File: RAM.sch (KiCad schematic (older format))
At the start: 9 parts

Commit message: Minor fixes and the gitignore was removed
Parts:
- added C?: 100n, symbol C
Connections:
- net +3V3: no longer C?.1, C?.1, U?.1 (VDD), U?.25 (VDD)
- net GNDD: now also C?.2
- net at C?.1, C?.1, C?.1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: now also C?.1, C?.1, U?.1 (VDD), U?.25 (VDD), C?.1
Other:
- moved on the sheet: C?
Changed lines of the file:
@@
 L C C?
 U 1 1 58E1D705
-P 4600 1350
-F 0 "C?" H 4625 1450 50  0000 L CNN
-F 1 "2.7u" H 4625 1250 50  0000 L CNN
-F 2 "" H 4638 1200 50  0001 C CNN
-F 3 "" H 4600 1350 50  0001 C CNN
-	1    4600 1350
+P 4600 1400
+F 0 "C?" H 4625 1500 50  0000 L CNN
+F 1 "2.7u" H 4625 1300 50  0000 L CNN
+F 2 "" H 4638 1250 50  0001 C CNN
+F 3 "" H 4600 1400 50  0001 C CNN
+	1    4600 1400
 	1    0    0    -1
 $EndComp
@@
 L C C?
 U 1 1 58E1D776
-P 4400 1350
-F 0 "C?" H 4425 1450 50  0000 L CNN
-F 1 "100n" H 4425 1250 50  0000 L CNN
-F 2 "" H 4438 1200 50  0001 C CNN
-F 3 "" H 4400 1350 50  0001 C CNN
-	1    4400 1350
+P 4400 1400
+F 0 "C?" H 4425 1500 50  0000 L CNN
+F 1 "100n" H 4425 1300 50  0000 L CNN
+F 2 "" H 4438 1250 50  0001 C CNN
+F 3 "" H 4400 1400 50  0001 C CNN
+	1    4400 1400
 	1    0    0    -1
 $EndComp
@@
 L GNDD #PWR?
 U 1 1 58E1D898
-P 4500 1500
-F 0 "#PWR?" H 4500 1250 50  0001 C CNN
-F 1 "GNDD" H 4500 1350 50  0000 C CNN
-F 2 "" H 4500 1500 50  0001 C CNN
-F 3 "" H 4500 1500 50  0001 C CNN
-	1    4500 1500
+P 4500 1600
+F 0 "#PWR?" H 4500 1350 50  0001 C CNN
+F 1 "GNDD" H 4500 1450 50  0000 C CNN
+F 2 "" H 4500 1600 50  0001 C CNN
+F 3 "" H 4500 1600 50  0001 C CNN
+	1    4500 1600
 	1    0    0    -1
 $EndComp
@@
 	4750 4900 4750 4750
 Wire Wire Line
-	4750 4750 5250 4750
-Connection ~ 4850 4750
-Connection ~ 4950 4750
-Connection ~ 5050 4750
-Connection ~ 5150 4750
-Wire Wire Line
 	5350 1200 5500 1200
 Wire Wire Line
-	3750 1200 5050 1200
+	3500 1200 5050 1200
 Connection ~ 4600 1200
-Wire Wire Line
-	4750 1650 5050 1650
 Wire Wire Line
 	4950 1650 4950 1200
 Connection ~ 4950 1200
-Wire Wire Line
-	5450 1650 5450 1200
 Connection ~ 5450 1200
-Wire Wire Line
-	3750 1500 4600 1500
-Connection ~ 4500 1500
-Connection ~ 4850 1650
+$Comp
+L C C?
+U 1 1 58E1DAA0
+P 3750 1400
+F 0 "C?" H 3775 1500 50  0000 L CNN
+F 1 "100n" H 3775 1300 50  0000 L CNN
+F 2 "" H 3788 1250 50  0001 C CNN
+F 3 "" H 3750 1400 50  0001 C CNN
+	1    3750 1400
+	1    0    0    -1
+$EndComp
+$Comp
+L C C?
+U 1 1 58E1DADF
+P 3950 1400
+F 0 "C?" H 3975 1500 50  0000 L CNN
+F 1 "100n" H 3975 1300 50  0000 L CNN
+F 2 "" H 3988 1250 50  0001 C CNN
+F 3 "" H 3950 1400 50  0001 C CNN
+	1    3950 1400
+	1    0    0    -1
+$EndComp
+$Comp
+L C C?
+U 1 1 58E1DB0D
+P 4200 1400
+F 0 "C?" H 4225 1500 50  0000 L CNN
+F 1 "100n" H 4225 1300 50  0000 L CNN
+F 2 "" H 4238 1250 50  0001 C CNN
+F 3 "" H 4200 1400 50  0001 C CNN
+	1    4200 1400
+	1    0    0    -1
+$EndComp
+Connection ~ 3950 1200
+Connection ~ 4400 1200
+$Comp
+L C C?
+U 1 1 58E1DD36
+P 5600 1600
+F 0 "C?" H 5625 1700 50  0000 L CNN
+F 1 "100n" H 5625 1500 50  0000 L CNN
+F 2 "" H 5638 1450 50  0001 C CNN
+F 3 "" H 5600 1600 50  0001 C CNN
+	1    5600 1600
+	1    0    0    -1
+$EndComp
+$Comp
+L GNDD #PWR?
+U 1 1 58E1DD7E
+P 5950 1850
+F 0 "#PWR?" H 5950 1600 50  0001 C CNN
+F 1 "GNDD" H 5950 1700 50  0000 C CNN
+F 2 "" H 5950 1850 50  0001 C CNN
+F 3 "" H 5950 1850 50  0001 C CNN
+	1    5950 1850
+	1    0    0    -1
+$EndComp
+$Comp
+L C C?
+U 1 1 58E1DDA1
+P 5950 1600
+F 0 "C?" H 5975 1700 50  0000 L CNN
+F 1 "100n" H 5975 1500 50  0000 L CNN
+F 2 "" H 5988 1450 50  0001 C CNN
+F 3 "" H 5950 1600 50  0001 C CNN
+	1    5950 1600
+	1    0    0    -1
+$EndComp
+Wire Wire Line
+	4950 1400 5950 1400
+Connection ~ 5600 1400
+Wire Wire Line
+	3750 1250 3750 1200
+Wire Wire Line
+	3950 1250 3950 1200
+Wire Wire Line
+	4400 1250 4400 1200
+Wire Wire Line
+	4600 1250 4600 1200
+Wire Wire Line
+	4600 1600 4600 1550
+Wire Wire Line
+	3500 1600 4600 1600
+Wire Wire Line
+	3750 1600 3750 1550
+Connection ~ 4500 1600
+Wire Wire Line
+	3950 1550 3950 1600
+Connection ~ 3950 1600
+Wire Wire Line
+	4400 1550 4400 1600
+Connection ~ 4400 1600
+Wire Wire Line
+	4200 1250 4200 1200
+Connection ~ 4200 1200
+Wire Wire Line
+	4200 1550 4200 1600
+Connection ~ 4200 1600
+$Comp
+L C C?
+U 1 1 58DF4B0B
+P 3500 1400
+F 0 "C?" H 3525 1500 50  0000 L CNN
+F 1 "100n" H 3525 1300 50  0000 L CNN
+F 2 "" H 3538 1250 50  0001 C CNN
+F 3 "" H 3500 1400 50  0001 C CNN
+	1    3500 1400
+	1    0    0    -1
+$EndComp
+Wire Wire Line
+	3500 1200 3500 1250
+Connection ~ 3750 1200
+Wire Wire Line
+	3500 1600 3500 1550
+Connection ~ 3750 1600
+Wire Wire Line
+	5600 1450 5600 1400
+Wire Wire Line
+	5950 1400 5950 1450
+Wire Wire Line
+	5950 1750 5950 1850
+Wire Wire Line
+	5950 1800 5600 1800
+Wire Wire Line
+	5600 1800 5600 1750
+Connection ~ 5950 1800
+Wire Wire Line
+	4750 1650 4750 1550
+Wire Wire Line
+	4750 1550 5250 1550
+Connection ~ 4950 1550
+Wire Wire Line
+	5250 1550 5250 1650
+Connection ~ 4950 1400
+Wire Wire Line
+	4850 1650 4850 1550
+Connection ~ 4850 1550
+Wire Wire Line
+	5050 1650 5050 1550
+Connection ~ 5050 1550
+Wire Wire Line
+	5150 1650 5150 1550
+Connection ~ 5150 1550
+Wire Wire Line
+	5250 4750 5250 4850
+Wire Wire Line
+	5250 4850 4750 4850
+Connection ~ 4750 4850
 $Comp
 L AS4C1M16S U?
@@
 	1    0    0    -1
 $EndComp
-Connection ~ 4950 1650
-Wire Wire Line
-	5150 1650 5450 1650
-Connection ~ 5250 1650
-Connection ~ 4750 1650
-$Comp
-L C C?
-U 1 1 58E1DAA0
-P 3750 1350
-F 0 "C?" H 3775 1450 50  0000 L CNN
-F 1 "100n" H 3775 1250 50  0000 L CNN
-F 2 "" H 3788 1200 50  0001 C CNN
-F 3 "" H 3750 1350 50  0001 C CNN
-	1    3750 1350
-	1    0    0    -1
-$EndComp
-$Comp
-L C C?
-U 1 1 58E1DADF
-P 3950 1350
-F 0 "C?" H 3975 1450 50  0000 L CNN
-F 1 "100n" H 3975 1250 50  0000 L CNN
-F 2 "" H 3988 1200 50  0001 C CNN
-F 3 "" H 3950 1350 50  0001 C CNN
-	1    3950 1350
-	1    0    0    -1
-$EndComp
-$Comp
-L C C?
-U 1 1 58E1DB0D
-P 4150 1350
-F 0 "C?" H 4175 1450 50  0000 L CNN
-F 1 "100n" H 4175 1250 50  0000 L CNN
-F 2 "" H 4188 1200 50  0001 C CNN
-F 3 "" H 4150 1350 50  0001 C CNN
-	1    4150 1350
-	1    0    0    -1
-$EndComp
-Connection ~ 3950 1200
-Connection ~ 4150 1200
-Connection ~ 4400 1200
-Connection ~ 3950 1500
-Connection ~ 4400 1500
-Connection ~ 4150 1500
-$Comp
-L C C?
-U 1 1 58E1DD36
-P 5600 1550
-F 0 "C?" H 5625 1650 50  0000 L CNN
-F 1 "100n" H 5625 1450 50  0000 L CNN
-F 2 "" H 5638 1400 50  0001 C CNN
-F 3 "" H 5600 1550 50  0001 C CNN
-	1    5600 1550
-	1    0    0    -1
-$EndComp
-$Comp
-L GNDD #PWR?
-U 1 1 58E1DD7E
-P 5600 1700
-F 0 "#PWR?" H 5600 1450 50  0001 C CNN
-F 1 "GNDD" H 5600 1550 50  0000 C CNN
-F 2 "" H 5600 1700 50  0001 C CNN
-F 3 "" H 5600 1700 50  0001 C CNN
-	1    5600 1700
-	1    0    0    -1
-$EndComp
-$Comp
-L C C?
-U 1 1 58E1DDA1
-P 5950 1550
-F 0 "C?" H 5975 1650 50  0000 L CNN
-F 1 "100n" H 5975 1450 50  0000 L CNN
-F 2 "" H 5988 1400 50  0001 C CNN
-F 3 "" H 5950 1550 50  0001 C CNN
-	1    5950 1550
-	1    0    0    -1
-$EndComp
-Wire Wire Line
-	5600 1700 5950 1700
-Wire Wire Line
-	5450 1400 5950 1400
-Connection ~ 5450 1400
-Connection ~ 5600 1400
+Wire Wire Line
+	4850 4750 4850 4850
+Connection ~ 4850 4850
+Wire Wire Line
+	4950 4750 4950 4850
+Connection ~ 4950 4850
+Wire Wire Line
+	5050 4750 5050 4850
+Connection ~ 5050 4850
+Wire Wire Line
+	5150 4750 5150 4850
+Connection ~ 5150 4850
 $EndSCHEMATC

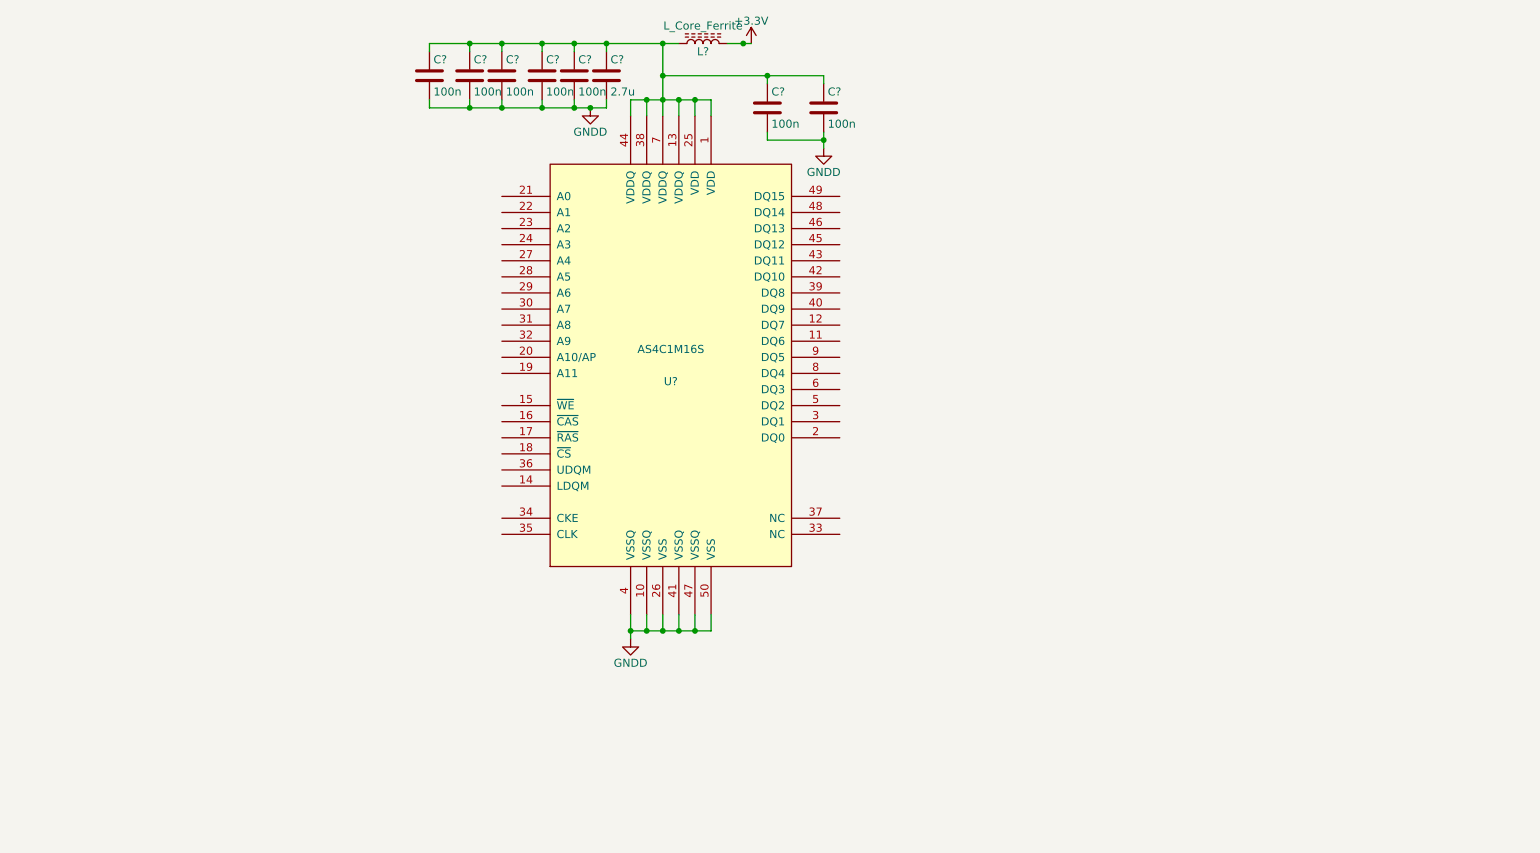
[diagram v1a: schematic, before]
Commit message: Reordered IO connections to FPGA
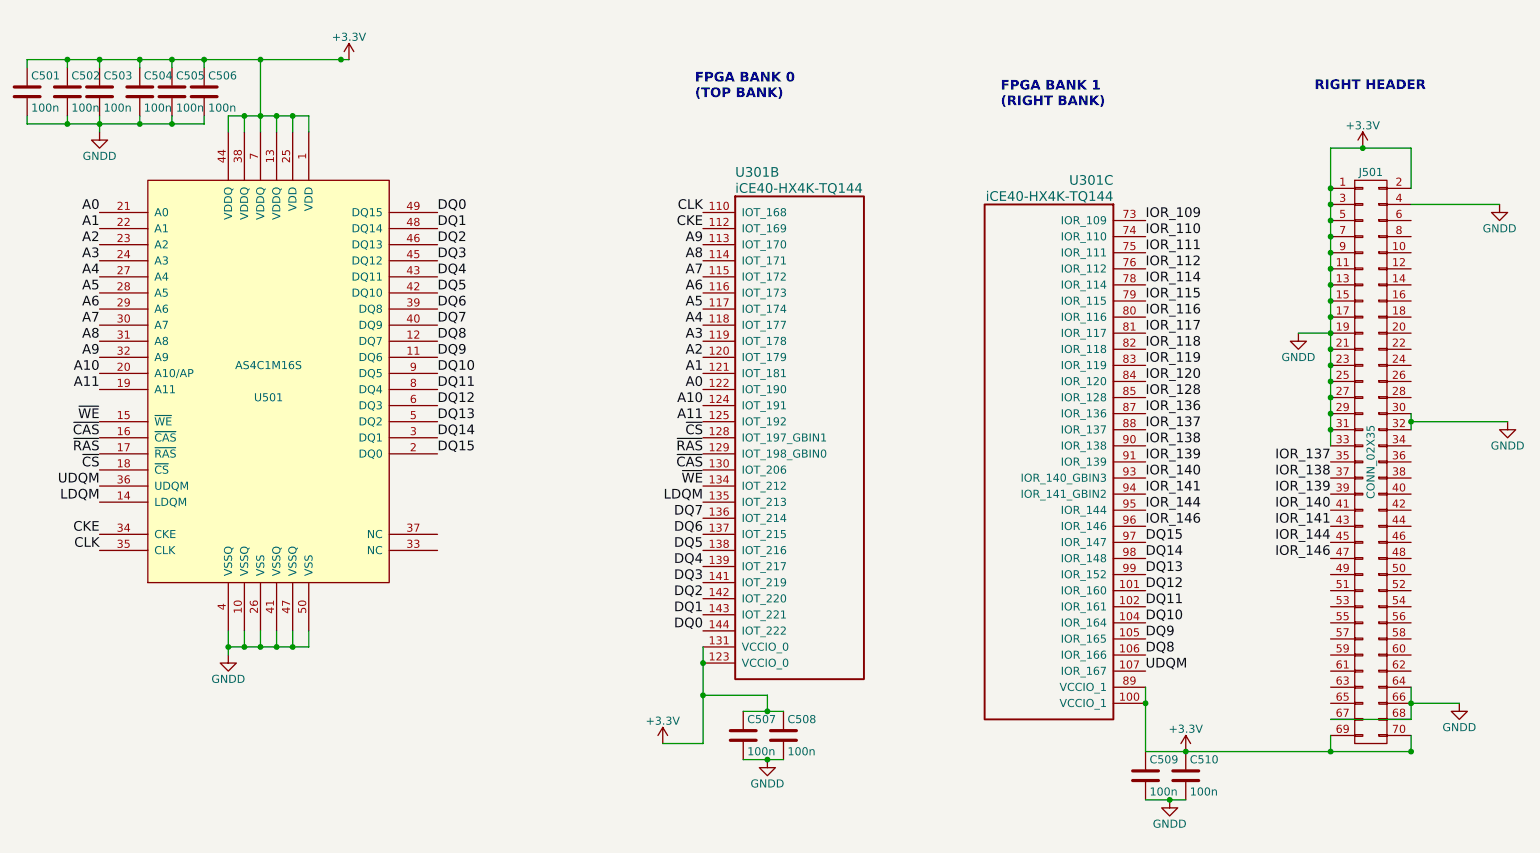
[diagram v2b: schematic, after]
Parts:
- removed C?: 2.7u, symbol C
- removed C?: 100n, symbol C
- removed L?: L_Core_Ferrite, symbol L_Core_Ferrite
- added C507, C508, C509, C510: 100n, symbol C
- added J501: CONN_02X35, symbol CONN_02X35
- added U301: iCE40-HX4K-TQ144, symbol iCE40-HX4K-TQ144
- gave numbers to parts that had none: 7
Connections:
- net GNDD is gone; now on net +3V3: C501.2, C502.2, C503.2, C504.2, C505.2, C506.2, U501.10 (VSSQ), U501.26 (VSS), U501.4 (VSSQ), U501.41 (VSSQ), U501.47 (VSSQ), U501.50 (VSS)
- net +3V3: now also C501.1, C502.1, C503.1, C504.1, C505.1, C506.1, U501.1 (VDD), U501.13 (VDDQ), U501.25 (VDD), U501.38 (VDDQ), U501.44 (VDDQ), U501.7 (VDDQ), C507.1, C507.2, C508.1, C508.2, C509.1, C509.2, C510.1, C510.2, J501.1 (P1), J501.11 (P11), J501.13 (P13), J501.15 (P15), J501.17 (P17), J501.19 (P19), J501.2 (P2), J501.21 (P21), J501.23 (P23), J501.25 (P25), J501.27 (P27), J501.29 (P29), J501.3 (P3), J501.30 (P30), J501.31 (P31), J501.32 (P32), J501.33 (P33), J501.4 (P4), J501.5 (P5), J501.64 (P64), J501.66 (P66), J501.67 (P67), J501.68 (P68), J501.69 (P69), J501.7 (P7), J501.70 (P70), J501.9 (P9), U301.100 (VCCIO_1), U301.123 (VCCIO_0), U301.131 (VCCIO_0), U301.89 (VCCIO_1)
- net DQ9: now reaches U501.11 (DQ6)
- net DQ9: now also U301.105 (IOR_165)
- net DQ8: now reaches U501.12 (DQ7)
- net DQ8: now also U301.106 (IOR_166)
- net LDQM: now reaches U501.14 (LDQM)
- net LDQM: now also U301.135 (IOT_213)
- net ~WE: now reaches U501.15 (~WE)
- net ~WE: now also U301.134 (IOT_212)
- net ~CAS: now reaches U501.16 (~CAS)
- net ~CAS: now also U301.130 (IOT_206)
- net ~RAS: now reaches U501.17 (~RAS)
- net ~RAS: now also U301.129 (IOT_198_GBIN0)
- net ~CS: now reaches U501.18 (~CS)
- net ~CS: now also U301.128 (IOT_197_GBIN1)
- net A11: now reaches U501.19 (A11)
- net A11: now also U301.125 (IOT_192)
- net DQ15: now reaches U501.2 (DQ0)
- net DQ15: now also U301.97 (IOR_147)
- net A10: now reaches U501.20 (A10/AP)
- net A10: now also U301.124 (IOT_191)
- net A0: now reaches U501.21 (A0)
- net A0: now also U301.122 (IOT_190)
- net A1: now reaches U501.22 (A1)
- net A1: now also U301.121 (IOT_181)
- net A2: now reaches U501.23 (A2)
- net A2: now also U301.120 (IOT_179)
- net A3: now reaches U501.24 (A3)
- net A3: now also U301.119 (IOT_178)
- net A4: now reaches U501.27 (A4)
- net A4: now also U301.118 (IOT_177)
- net A5: now reaches U501.28 (A5)
- net A5: now also U301.117 (IOT_174)
- net A6: now reaches U501.29 (A6)
- net A6: now also U301.116 (IOT_173)
- net DQ14: now reaches U501.3 (DQ1)
- net DQ14: now also U301.98 (IOR_148)
- net A7: now reaches U501.30 (A7)
- net A7: now also U301.115 (IOT_172)
- net A8: now reaches U501.31 (A8)
- net A8: now also U301.114 (IOT_171)
- net A9: now reaches U501.32 (A9)
- net A9: now also U301.113 (IOT_170)
- net CKE: now reaches U501.34 (CKE)
- net CKE: now also U301.112 (IOT_169)
- net CLK: now reaches U501.35 (CLK)
- net CLK: now also U301.110 (IOT_168)
- net UDQM: now reaches U501.36 (UDQM)
- net UDQM: now also U301.107 (IOR_167)
- net DQ6: now reaches U501.39 (DQ8)
- net DQ6: now also U301.137 (IOT_215)
- net DQ7: now reaches U501.40 (DQ9)
- net DQ7: now also U301.136 (IOT_214)
- net DQ5: now reaches U501.42 (DQ10)
- net DQ5: now also U301.138 (IOT_216)
- net DQ4: now reaches U501.43 (DQ11)
- net DQ4: now also U301.139 (IOT_217)
- net DQ3: now reaches U501.45 (DQ12)
- net DQ3: now also U301.141 (IOT_219)
- net DQ2: now reaches U501.46 (DQ13)
- net DQ2: now also U301.142 (IOT_220)
- net DQ1: now reaches U501.48 (DQ14)
- net DQ1: now also U301.143 (IOT_221)
- net DQ0: now reaches U501.49 (DQ15)
- net DQ0: now also U301.144 (IOT_222)
- net DQ13: now reaches U501.5 (DQ2)
- net DQ13: now also U301.99 (IOR_152)
- net DQ12: now reaches U501.6 (DQ3)
- net DQ12: now also U301.101 (IOR_160)
- net DQ11: now reaches U501.8 (DQ4)
- net DQ11: now also U301.102 (IOR_161)
- net DQ10: now reaches U501.9 (DQ5)
- net DQ10: now also U301.104 (IOR_164)
- new net IOR_109: U301.73 (IOR_109)
- new net IOR_110: U301.74 (IOR_110)
- new net IOR_111: U301.75 (IOR_111)
- new net IOR_112: U301.76 (IOR_112)
- new net IOR_114: U301.78 (IOR_114)
- new net IOR_115: U301.79 (IOR_115)
- new net IOR_116: U301.80 (IOR_116)
- new net IOR_117: U301.81 (IOR_117)
- new net IOR_118: U301.82 (IOR_118)
- new net IOR_119: U301.83 (IOR_119)
- new net IOR_120: U301.84 (IOR_120)
- new net IOR_128: U301.85 (IOR_128)
- new net IOR_136: U301.87 (IOR_136)
- new net IOR_137: J501.35 (P35), U301.88 (IOR_137)
- new net IOR_138: J501.37 (P37), U301.90 (IOR_138)
- new net IOR_139: J501.39 (P39), U301.91 (IOR_139)
- new net IOR_140: J501.41 (P41), U301.93 (IOR_140_GBIN3)
- new net IOR_141: J501.43 (P43), U301.94 (IOR_141_GBIN2)
- new net IOR_144: J501.45 (P45), U301.95 (IOR_144)
- new net IOR_146: J501.47 (P47), U301.96 (IOR_146)
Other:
- note added: "FPGA BANK 0\n(TOP BANK)"
- note added: "FPGA BANK 1\n(RIGHT BANK)"
- note added: "RIGHT HEADER"
- moved on the sheet: C501, C502, C503, C504, C505, C506, U501

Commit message: Added part number and specifications on all sheets
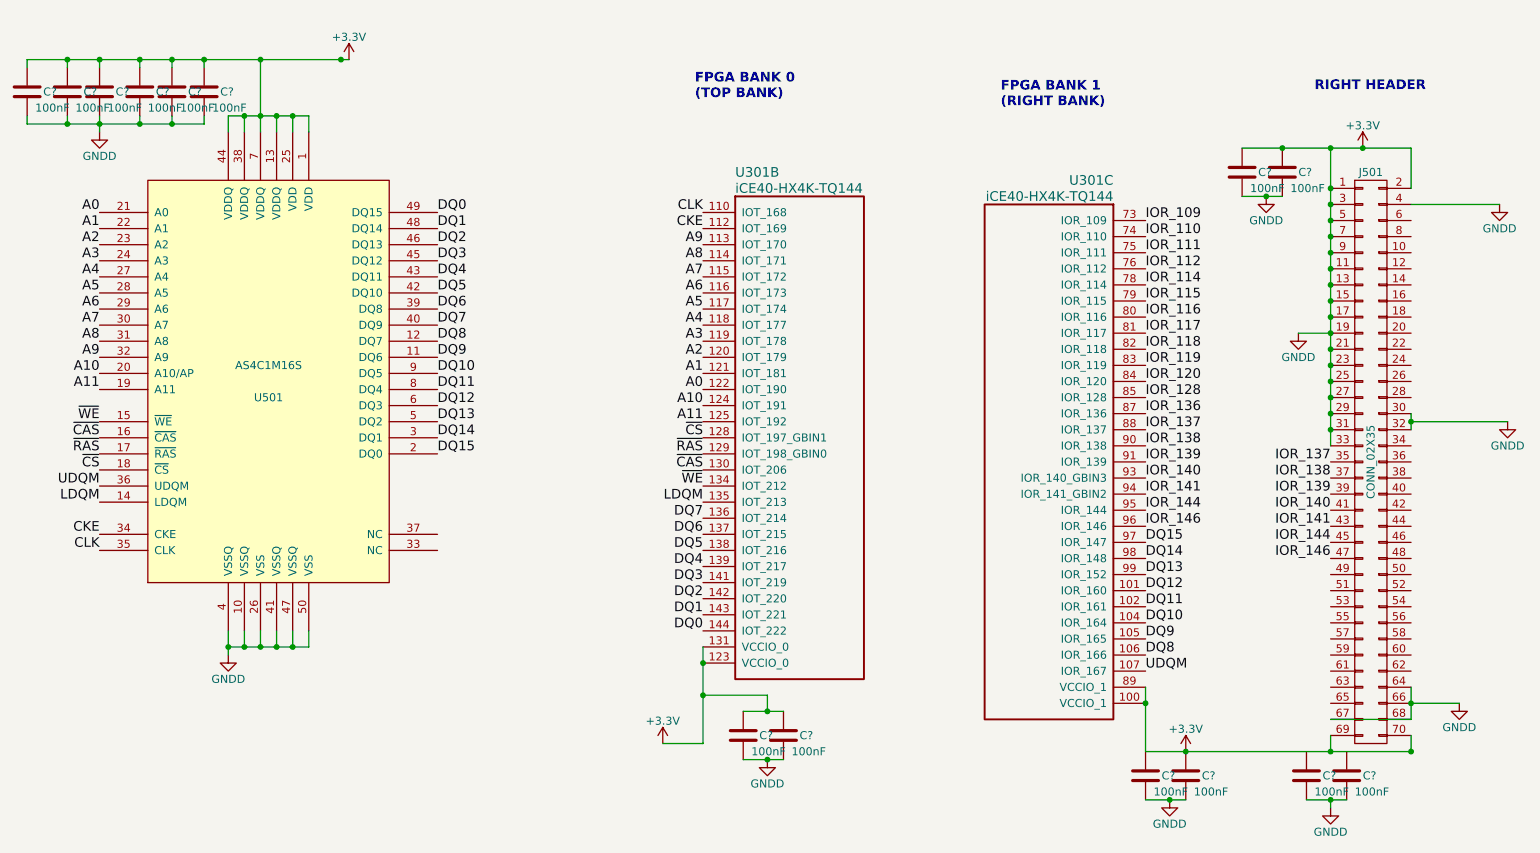
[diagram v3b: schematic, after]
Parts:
- removed C501, C502, C503, C504, C505, C506, C507, C508, C509, C510: 100n, symbol C
- added C? (x14): 100nF, Capacitors_SMD:C_0603_HandSoldering, symbol C
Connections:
- net +3V3: now also C?.1, C?.1, C?.1, C?.1, C?.1, C?.1, C?.1, C?.1, C?.1, C?.1, C?.1, C?.1, C?.2, C?.2, C?.2, C?.2, C?.2, C?.2, C?.2, C?.2, C?.2, C?.2, C?.2, C?.2, C?.2, C?.2
